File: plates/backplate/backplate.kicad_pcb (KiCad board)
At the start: 2 copper layers, 33.2 x 78.4 mm, 2 parts

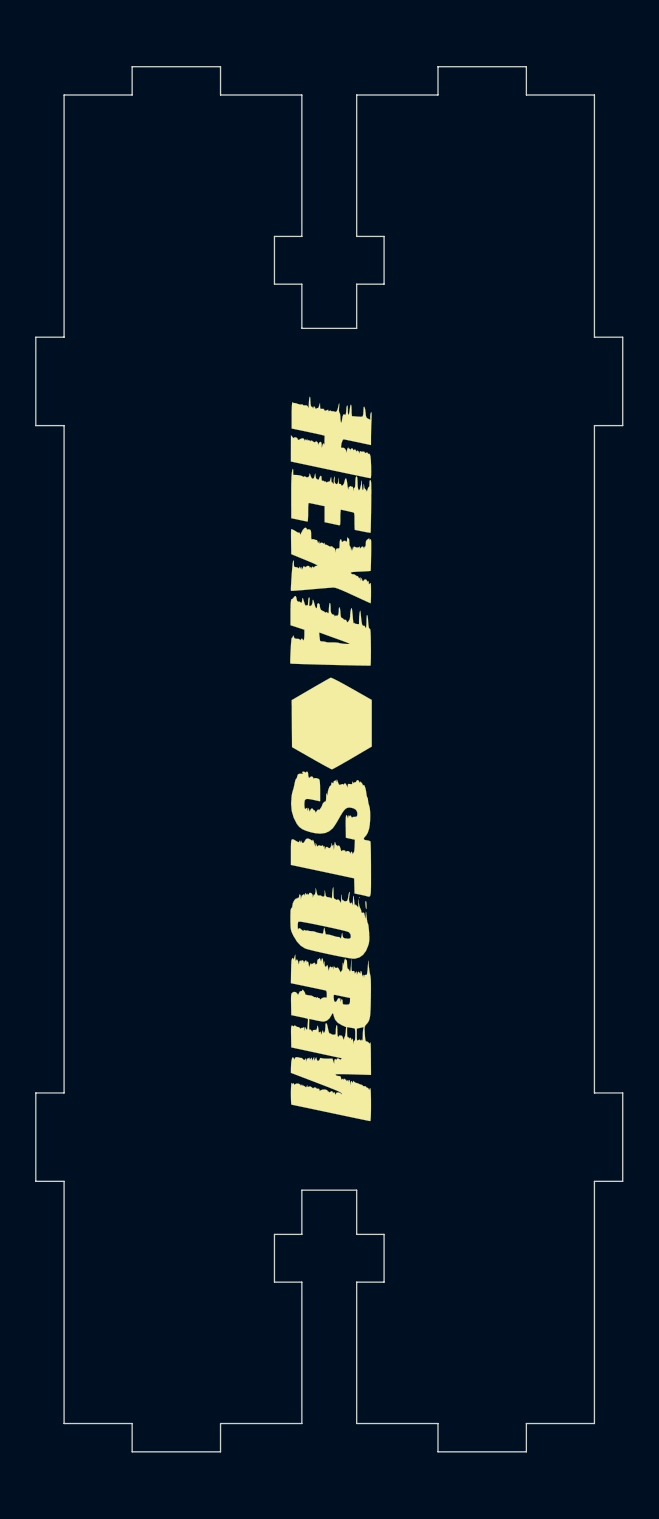
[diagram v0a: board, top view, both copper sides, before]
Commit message: improved bom changed export settings
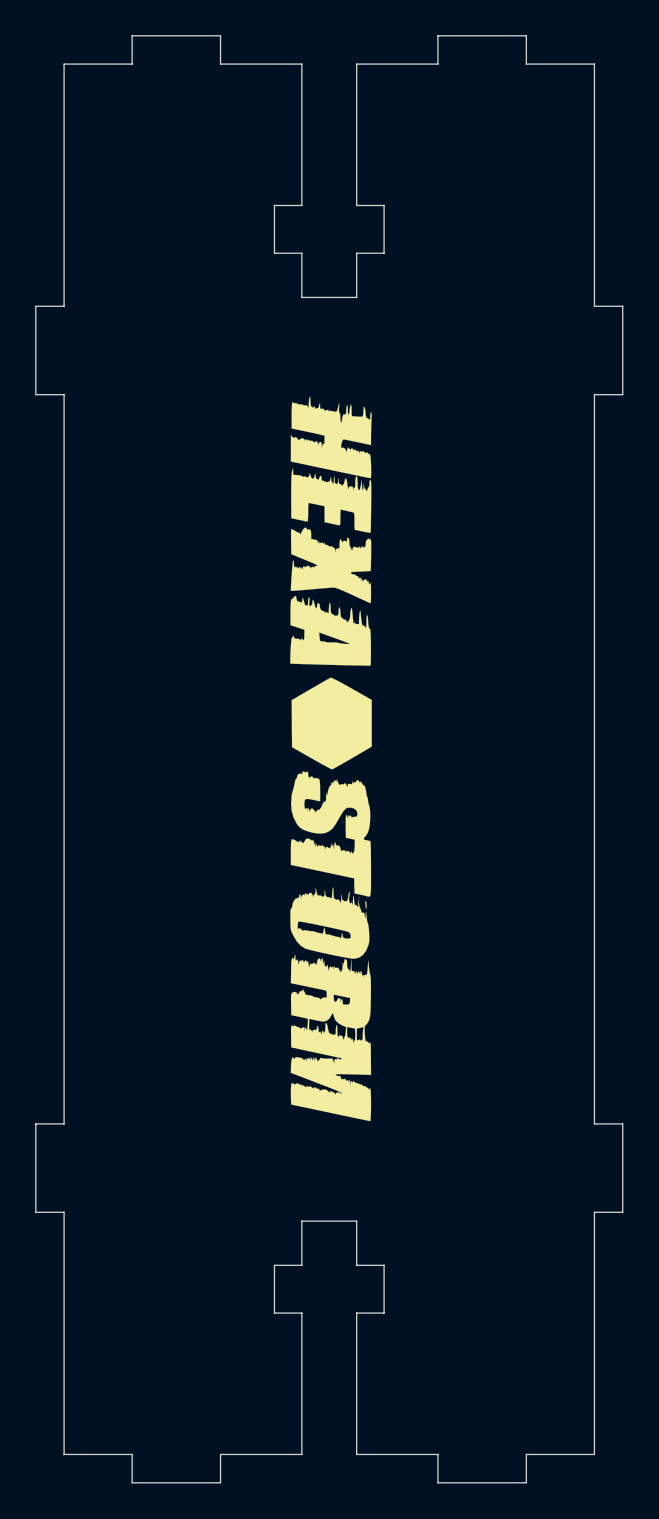
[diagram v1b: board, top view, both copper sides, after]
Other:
- board size 33.2 x 78.4 mm -> 33.2 x 81.8 mm

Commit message: added design of june
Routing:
- net (no net): vias 0 -> 3
- added copper zone on F.Cu, net (none)
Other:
- board size 33.2 x 81.8 mm -> 25.2 x 55.1 mm
- net class Default removed
- board text added: "HEXASTORM"
